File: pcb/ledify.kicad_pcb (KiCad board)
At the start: 4 copper layers, 35.5 x 52.5 mm, 76 parts, among them J1 Conn_01x01_Pin, J2 USB_C_Receptacle_USB2.0_16P, J3 Conn_01x01_Pin, J4 Conn_01x01_Pin, Q1 2N7002K, SW1 TS-1088-AR02016, SW2 TS-1088-AR02016, U1 ESP32-C6_C5364646, U2 USBLC6-2P6, U3 AP63203WU, U4 FUSB302BMPX, U5 W25Q128JVP, U6 LM61495QRPHRQ1, U7 BMI323, U8 BMP581, X1 XL2EL89COI-111YLC-40M, X2 Q13FC1350000400

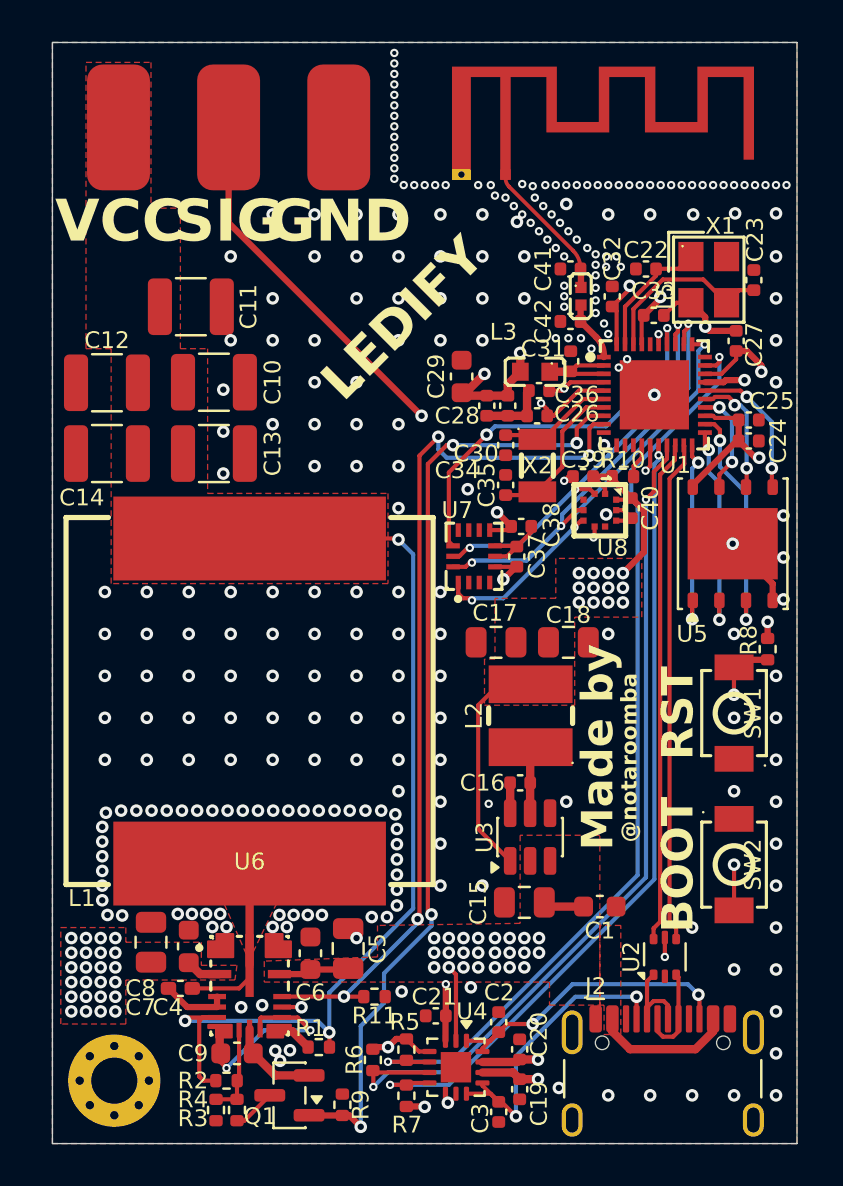
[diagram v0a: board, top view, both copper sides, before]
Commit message: add light sensor and i2s mic, fix ground return paths, update journal
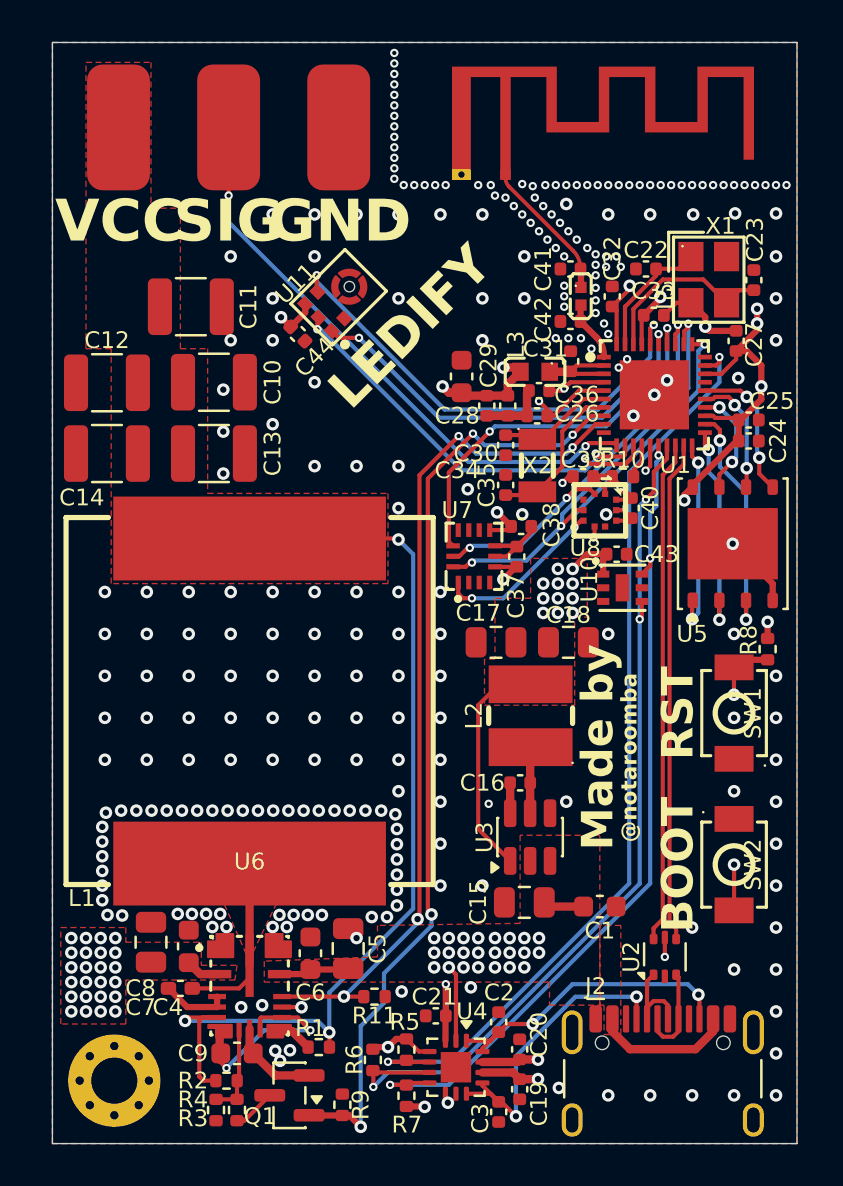
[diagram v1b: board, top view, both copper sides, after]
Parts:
- added C43: 100nF, Capacitor_SMD:C_0402_1005Metric, F.Cu at (81.2, 60.0)
- added C44: 100nF, Capacitor_SMD:C_0402_1005Metric, F.Cu at (66.0, 49.5)
- added U10: OPT4001DNPRQ1, lcsc:USON-6_L2.0-W2.0-P0.65-BL-EP, F.Cu at (81.5, 61.6)
- added U11: ICS-43434_C5656610, lcsc:MIC-SMD_6P-L3.5-W2.7-P0.90-BL, F.Cu at (67.9, 47.8)
- C6: value 470nF -> 470nF 50V
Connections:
- net /USB_PD_SCL renamed /I2C_SCL
- net /USB_PD_SDA renamed /I2C_SDA
- U1 pad 11: unconnected-(U1-MTDI-Pad11) -> /LED_CON
- U1 pad 12: unconnected-(U1-MTCK-Pad12) -> /MIC_OUT
- U1 pad 13: unconnected-(U1-MTDO-Pad13) -> /CS_BARO
- U1 pad 27: /LED_CON -> unconnected-(U1-GPIO15-Pad27)
- U1 pad 35: /CS_BARO -> /MIC_CS
- U1 pad 36: unconnected-(U1-SDIO_DATA3-Pad36) -> /MIC_SCK
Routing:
- net /MIC_SCK: track 0.00 -> 23.2 mm, vias 0 -> 2
- net /MIC_CS: track 0.00 -> 20.2 mm, vias 0 -> 2
- net /MIC_OUT: track 0.00 -> 19.1 mm, vias 0 -> 2
- net /CS_BARO: track 15.1 -> 7.56 mm
- net /LED_CON: track 35.6 -> 28.2 mm
- net /CHIP_EN: track 27.4 -> 33.4 mm
- net +3V3: track 64.6 -> 69.7 mm, vias 28 -> 31
- net /LED_ENABLE: track 42.5 -> 40.7 mm
- net /I2C_SDA: track 39.4 -> 40.3 mm, vias 2 -> 3
- net /I2C_SCL: track 41.7 -> 42.6 mm, vias 2 -> 3
- net /SPI_SCK: track 19.0 -> 19.6 mm
- net GND: track 22.6 -> 22.7 mm, vias 274 -> 259
- removed copper zone on In1.Cu, net LED_VCC
